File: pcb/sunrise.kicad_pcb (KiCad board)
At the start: 2 copper layers, 6 parts, among them J1 Conn_01x15_Female, J3 Conn_01x04_Female, Q1 TSM2302CX, Q2 TSM2302CX, Q3 TSM2302CX

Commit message: Updated schematic and footprints
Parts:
- added J2: Conn_01x15_Female, Connector_PinSocket_2.54mm:PinSocket_1x15_P2.54mm_Vertical, F.Cu at (116.8, 97.8)
- added R2: R, Resistor_SMD:R_0805_2012Metric, F.Cu at (95.2, 85.1)
- added R3: R, Resistor_SMD:R_0805_2012Metric, F.Cu at (87.6, 85.1)
- added U1: MCP1703A-5002_SOT223, Package_TO_SOT_SMD:SOT-223-3_TabPin2, F.Cu at (119.4, 87.6)
- J1: footprint Connector_PinHeader_1.27mm:PinHeader_1x15_P1.27mm_Vertical -> Connector_PinSocket_2.54mm:PinSocket_1x15_P2.54mm_Vertical
- moved J1 59.2 mm to (116.8, 77.5), turned to -90 degrees
- moved R1 50.6 mm to (102.9, 85.1), turned to 180 degrees
- moved Q1 49.4 mm to (102.9, 90.2)
- moved Q2 48.3 mm to (95.2, 90.2)
- moved Q3 44.5 mm to (87.6, 90.2)
- moved J3 22.9 mm to (80.0, 86.4)
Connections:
- Q2 pad 1: /Green_IO -> Net-(Q2-Pad1)
- Q3 pad 1: /Blue_IO -> Net-(Q3-Pad1)
- R1 pad 1: /Red_IO -> unconnected-(R1-Pad1)
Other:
- board outline added: 52.1 x 27.9 mm

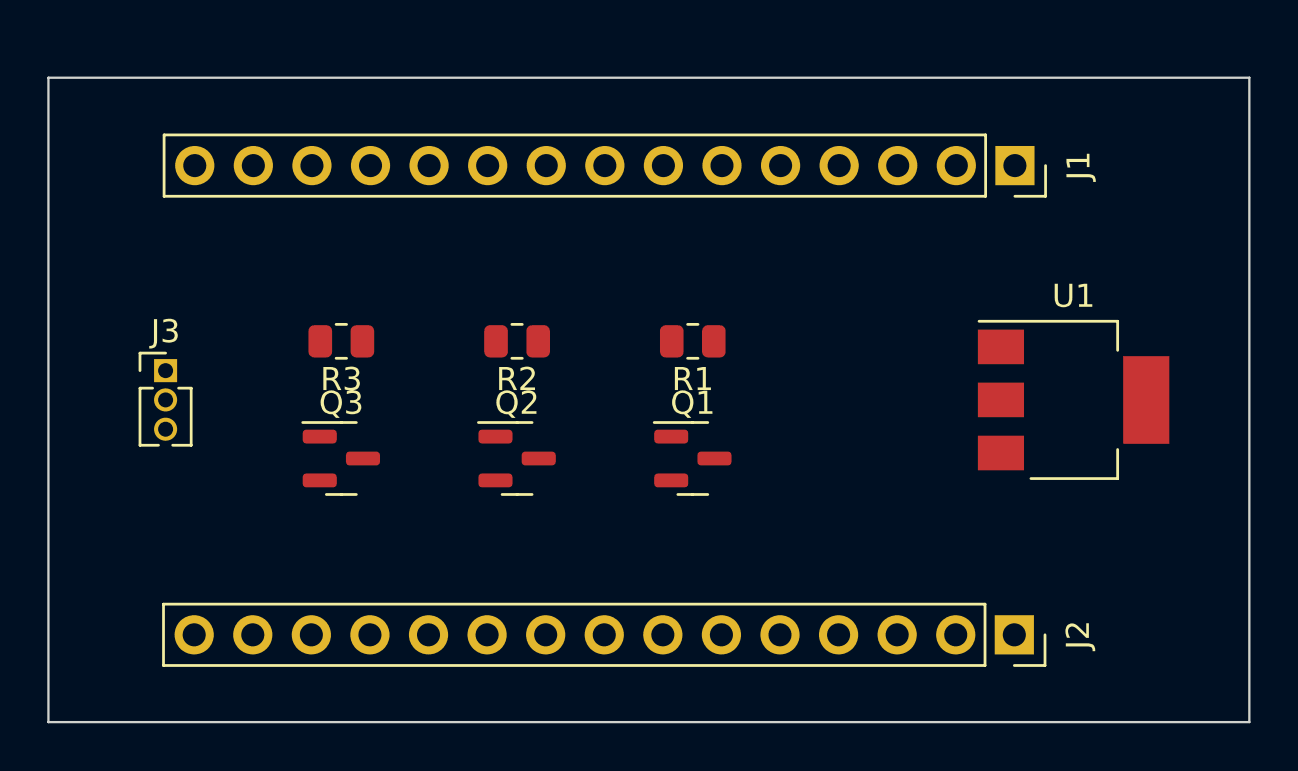
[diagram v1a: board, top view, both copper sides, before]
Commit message: Corrected schematic and finished layout
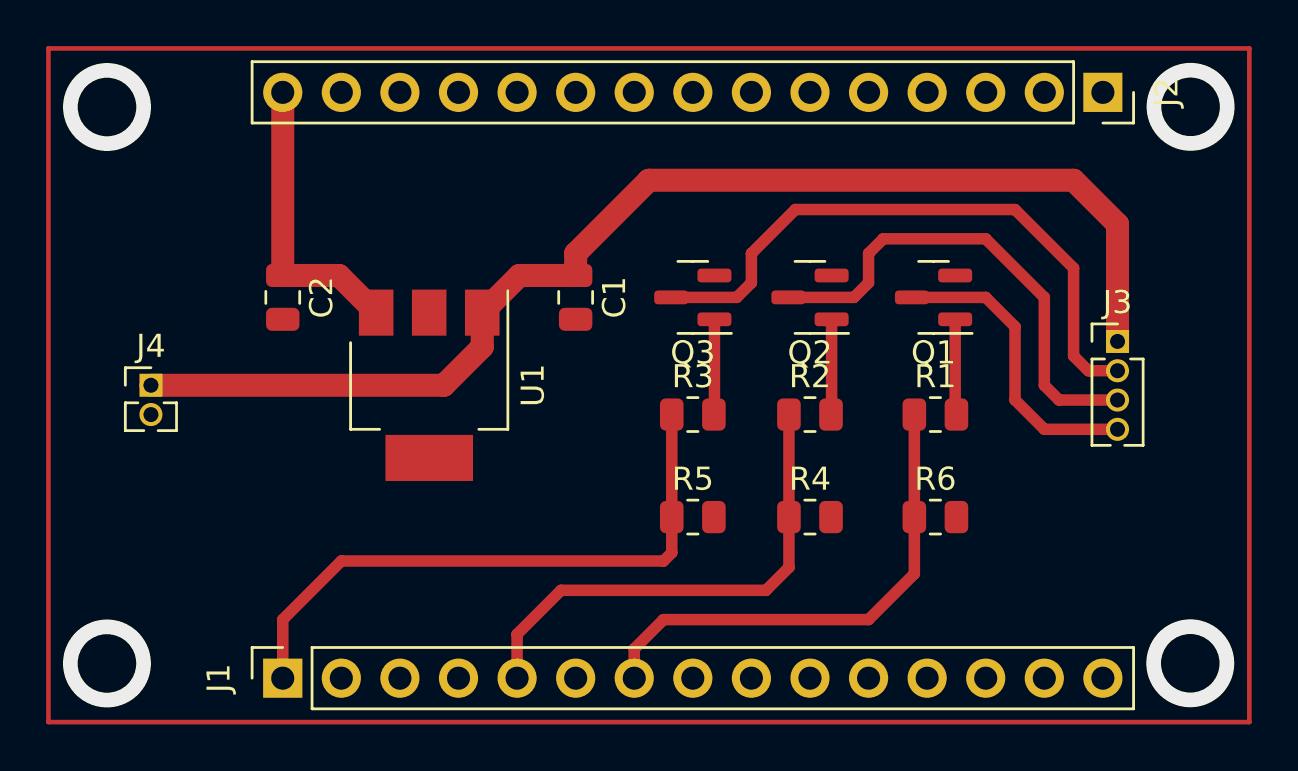
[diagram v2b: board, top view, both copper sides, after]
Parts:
- added C1: 10uF, Capacitor_SMD:C_0805_2012Metric, F.Cu at (97.8, 83.2)
- added C2: 10uF, Capacitor_SMD:C_0805_2012Metric, F.Cu at (85.1, 83.2)
- added J4: Conn_01x02_Female, Connector_PinHeader_1.27mm:PinHeader_1x02_P1.27mm_Vertical, F.Cu at (79.4, 87.0)
- added R4: 5k6, Resistor_SMD:R_0805_2012Metric, F.Cu at (108.0, 92.7)
- added R5: 5k6, Resistor_SMD:R_0805_2012Metric, F.Cu at (102.9, 92.7)
- added R6: 5k6, Resistor_SMD:R_0805_2012Metric, F.Cu at (113.4, 92.7)
- J3: footprint Connector_PinHeader_1.27mm:PinHeader_1x03_P1.27mm_Vertical -> Connector_PinHeader_1.27mm:PinHeader_1x04_P1.27mm_Vertical
- R1, R2, R3: value R -> 560
- moved J3 41.3 mm to (121.3, 85.1)
- moved J1 38.8 mm to (85.1, 99.7), turned to 90 degrees
- moved U1 27.9 mm to (91.4, 87.0), turned to -90 degrees
- moved J2 23.8 mm to (120.7, 74.3)
- moved Q3 16.8 mm to (102.9, 83.2), turned to 180 degrees
- moved R3 15.6 mm to (102.9, 88.3), turned to 0 degrees
- moved Q2 14.5 mm to (108.0, 83.2), turned to 180 degrees
- moved R2 13.1 mm to (108.0, 88.3), turned to 0 degrees
- moved Q1 12.6 mm to (113.3, 83.2), turned to 180 degrees
- moved R1 11.0 mm to (113.4, 88.3), turned to 0 degrees
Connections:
- J1 pad 1: /Red_IO -> /BLUE_IO
- J1 pad 5: unconnected-(J1-Pad5) -> /GREEN_IO
- J1 pad 7: unconnected-(J1-Pad7) -> /RED_IO
- J2 pad 14: unconnected-(J2-Pad14) -> GND
- J2 pad 15: unconnected-(J2-Pad15) -> +5V
- Q1 pad 3: Net-(Q1-Pad3) -> Net-(J3-Pad4)
- R1 pad 1: unconnected-(R1-Pad1) -> /RED_IO
- R2 pad 1: unconnected-(R2-Pad1) -> /GREEN_IO
- R3 pad 1: unconnected-(R3-Pad1) -> /BLUE_IO
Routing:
- net +12V: track 0.00 -> 52.9 mm
- net Net-(J3-Pad2): track 0.00 -> 26.8 mm
- net /BLUE_IO: track 0.00 -> 26.6 mm
- net /RED_IO: track 0.00 -> 21.7 mm
- net /GREEN_IO: track 0.00 -> 21.5 mm
- net Net-(J3-Pad3): track 0.00 -> 21.2 mm
- net Net-(J3-Pad4): track 0.00 -> 13.1 mm
- net +5V: track 0.00 -> 12.7 mm
- net Net-(Q1-Pad1): track 0.00 -> 4.15 mm
- net Net-(Q3-Pad1): track 0.00 -> 4.14 mm
- net Net-(Q2-Pad1): track 0.00 -> 4.14 mm
- net (no net): vias 0 -> 4
- added copper zone on F.Cu, net GND
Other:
- board outline removed

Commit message: Final
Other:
- board outline added: 52.1 x 29.2 mm
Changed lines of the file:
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@@
     (property "Sheetname" "")
     (attr smd)
-    (fp_text reference "R6" (at 0 -1.65) (layer "F.SilkS")
+    (fp_text reference "R6" (at -2.6435 0) (layer "F.SilkS")
       (effects (font (size 1 1) (thickness 0.15)))
     )
@@
     (property "Sheetname" "")
     (attr smd)
-    (fp_text reference "R3" (at 0 -1.65) (layer "F.SilkS")
+    (fp_text reference "R3" (at -3.175 0) (layer "F.SilkS")
       (effects (font (size 1 1) (thickness 0.15)))
     )
@@
     (property "Sheetname" "")
     (attr smd)
-    (fp_text reference "R2" (at 0 -1.65) (layer "F.SilkS")
+    (fp_text reference "R2" (at -2.54 0) (layer "F.SilkS")
       (effects (font (size 1 1) (thickness 0.15)))
     )
@@
     (property "Sheetname" "")
     (attr smd)
-    (fp_text reference "R5" (at 0 -1.65) (layer "F.SilkS")
+    (fp_text reference "R5" (at -3.175 0) (layer "F.SilkS")
       (effects (font (size 1 1) (thickness 0.15)))
     )
@@
     (property "Sheetname" "")
     (attr smd)
-    (fp_text reference "R4" (at 0 -1.65) (layer "F.SilkS")
+    (fp_text reference "R4" (at -2.54 0) (layer "F.SilkS")
       (effects (font (size 1 1) (thickness 0.15)))
     )
@@
     (property "Sheetname" "")
     (attr smd)
-    (fp_text reference "R1" (at 0 -1.65) (layer "F.SilkS")
+    (fp_text reference "R1" (at -2.6435 0) (layer "F.SilkS")
       (effects (font (size 1 1) (thickness 0.15)))
     )
@@
     )
   )
-  (gr_rect (start 74.93 101.6) (end 127 72.39) (layer "F.Cu") (width 0.2) (fill none))
+  (gr_rect (start 74.93 101.6) (end 127 72.39) (layer "Edge.Cuts") (width 0.2) (fill none))
   (via (at 124.452319 74.922319) (size 3.81) (drill 2.54) (layers "F.Cu" "B.Cu") (free) (net 0))
   (via (at 124.438991 99.049495) (size 3.81) (drill 2.54) (layers "F.Cu" "B.Cu") (free) (net 0))

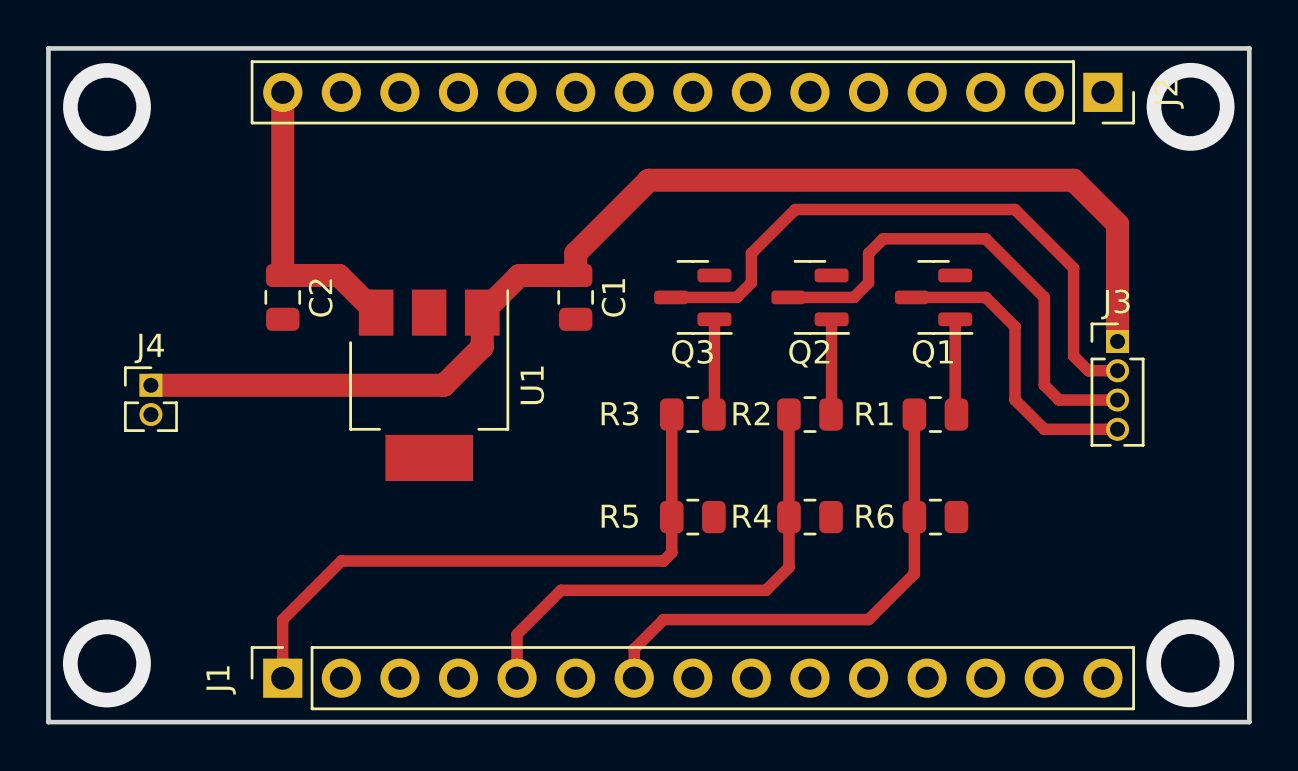
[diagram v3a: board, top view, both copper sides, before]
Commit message: Added IR receiver
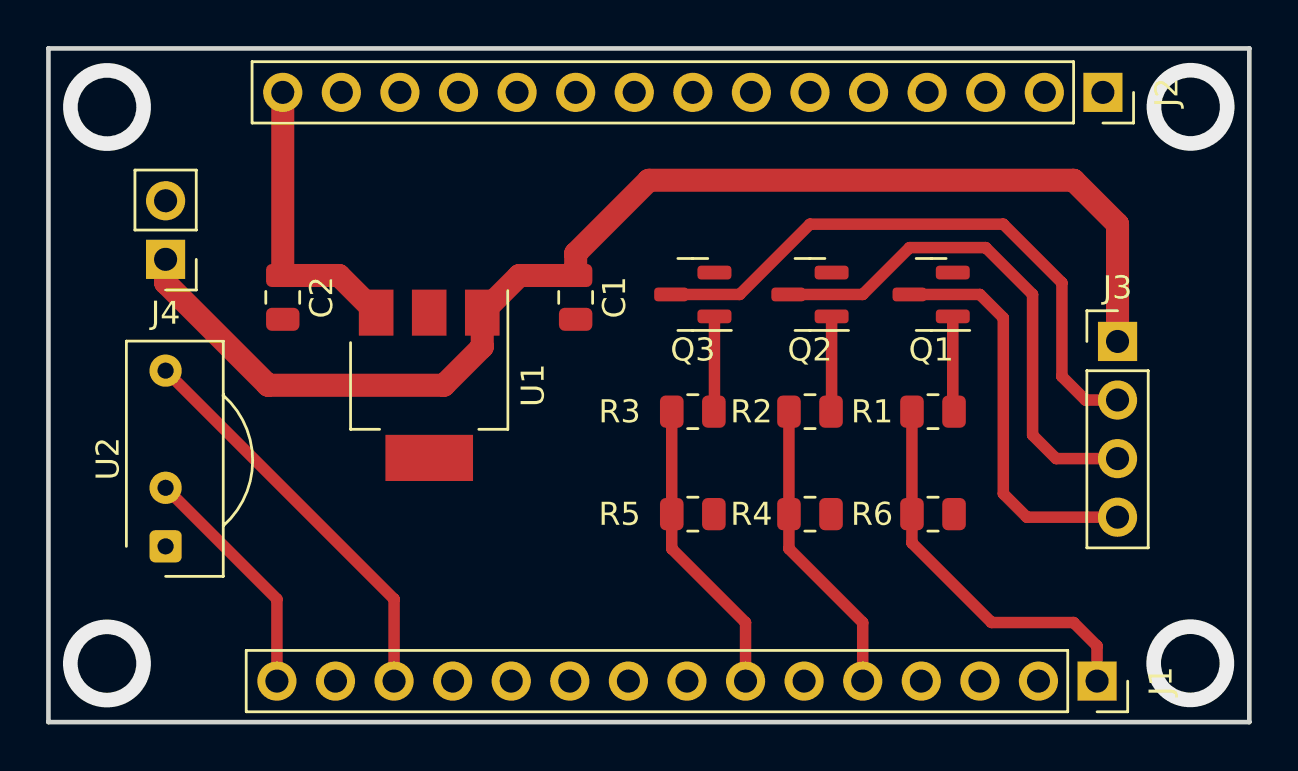
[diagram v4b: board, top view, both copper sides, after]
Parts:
- added U2: TSOP312xx, OptoDevice:Vishay_CAST-3Pin, F.Cu at (80.0, 94.0)
- J3: footprint Connector_PinHeader_1.27mm:PinHeader_1x04_P1.27mm_Vertical -> Connector_PinHeader_2.54mm:PinHeader_1x04_P2.54mm_Vertical
- J4: footprint Connector_PinHeader_1.27mm:PinHeader_1x02_P1.27mm_Vertical -> Connector_PinHeader_2.54mm:PinHeader_1x02_P2.54mm_Vertical
- moved J1 35.3 mm to (120.4, 99.8), turned to -90 degrees
- moved J4 5.50 mm to (80.0, 81.5), turned to 180 degrees
- moved Q1 0.16 mm to (113.2, 83.1)
- moved R1 0.16 mm to (113.3, 88.1)
- moved R6 0.16 mm to (113.3, 92.6)
- moved Q2 0.13 mm to (108.0, 83.1)
- moved Q3 0.13 mm to (102.9, 83.1)
- moved R2 0.13 mm to (108.0, 88.1)
- moved R3 0.13 mm to (102.9, 88.1)
- moved R4 0.13 mm to (108.0, 92.6)
- moved R5 0.13 mm to (102.9, 92.6)
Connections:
- J1 pad 1: /BLUE_IO -> /RED_IO
- J1 pad 13: unconnected-(J1-Pad13) -> /IR_D
- J1 pad 14: unconnected-(J1-Pad14) -> GND
- J1 pad 15: unconnected-(J1-Pad15) -> /+3.3V
- J1 pad 7: /RED_IO -> /BLUE_IO
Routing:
- net /IR_D: track 0.00 -> 17.6 mm
- net /BLUE_IO: track 26.6 -> 13.0 mm
- net /+3.3V: track 0.00 -> 10.4 mm
- net /GREEN_IO: track 21.5 -> 13.0 mm
- net /RED_IO: track 21.7 -> 17.1 mm
- net Net-(J3-Pad4): track 13.1 -> 17.5 mm
- net +12V: track 52.9 -> 55.1 mm
- net Net-(J3-Pad3): track 21.2 -> 22.5 mm
- net Net-(J3-Pad2): track 26.8 -> 26.2 mm
- removed copper zone on F.Cu, net GND

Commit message: Updated pcb
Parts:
- moved U2 1.02 mm to (80.0, 95.0)
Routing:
- added copper zone on F.Cu, net GND
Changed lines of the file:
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@@
   )
   (footprint "OptoDevice:Vishay_CAST-3Pin" (layer "F.Cu")
-    (at 80.01 93.98 90)
+    (at 80.01 94.996 90)
     (descr "IR Receiver Vishay TSOP-xxxx, CAST package, see https://www.vishay.com/docs/82493/tsop311.pdf")
     (tags "IRReceiverVishayTSOP-xxxx CAST")
@@
   (segment (start 92.075 86.995) (end 93.74 85.33) (width 1) (layer "F.Cu") (net 7))
   (segment (start 119.38 78.105) (end 121.285 80.01) (width 1) (layer "F.Cu") (net 7))
-  (segment (start 80.01 86.36) (end 89.916 96.266) (width 0.5) (layer "F.Cu") (net 18))
-  (segment (start 89.916 96.266) (end 89.916 99.822) (width 0.5) (layer "F.Cu") (net 18))
-  (segment (start 80.01 91.44) (end 84.836 96.266) (width 0.5) (layer "F.Cu") (net 19))
-  (segment (start 84.836 96.266) (end 84.836 99.822) (width 0.5) (layer "F.Cu") (net 19))
+  (segment (start 89.916 96.012) (end 89.916 99.822) (width 0.5) (layer "F.Cu") (net 18))
+  (segment (start 80.01 87.376) (end 81.28 87.376) (width 0.5) (layer "F.Cu") (net 18))
+  (segment (start 81.28 87.376) (end 89.916 96.012) (width 0.5) (layer "F.Cu") (net 18))
+  (segment (start 80.01 92.456) (end 82.296 92.456) (width 0.5) (layer "F.Cu") (net 19))
+  (segment (start 82.296 92.456) (end 84.836 94.996) (width 0.5) (layer "F.Cu") (net 19))
+  (segment (start 84.836 94.996) (end 84.836 99.822) (width 0.5) (layer "F.Cu") (net 19))
   (segment (start 103.8075 88.113) (end 103.7825 88.138) (width 0.5) (layer "F.Cu") (net 20))
   (segment (start 103.8075 84.008) (end 103.8075 88.113) (width 0.5) (layer "F.Cu") (net 20))
@@
   (segment (start 85.09 82.235) (end 85.09 74.295) (width 1) (layer "F.Cu") (net 24))
   (segment (start 87.53 82.235) (end 89.14 83.845) (width 1) (layer "F.Cu") (net 24))
+  (zone (net 1) (net_name "GND") (layer "F.Cu") (hatch edge 0.508)
+    (connect_pads (clearance 0.12))
+    (min_thickness 0.254) (filled_areas_thickness no)
+    (fill yes (thermal_gap 0.508) (thermal_bridge_width 0.508))
+    (polygon
+      (pts
+        (xy 127 101.6)
+        (xy 74.93 101.6)
+        (xy 74.93 72.39)
+        (xy 127 72.39)
+      )
+    )
+  )
 )

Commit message: Final layout
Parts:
- added R7: 10k, Resistor_SMD:R_0805_2012Metric, F.Cu at (89.9, 96.8)
- added R8: 10k, Resistor_SMD:R_0805_2012Metric, F.Cu at (120.4, 95.4)
- added SW1: SW_SPDT, MattisLib:SS 13PLP, F.Cu at (123.2, 86.9)
- moved J3 3.77 mm to (118.1, 83.1)
- moved R1 1.63 mm to (111.7, 88.1)
- moved R6 1.63 mm to (111.7, 92.6)
- moved Q1 1.63 mm to (111.6, 83.1)
- moved Q2 1.63 mm to (106.3, 83.1)
- moved Q3 1.63 mm to (101.2, 83.1)
- moved R2 1.63 mm to (106.3, 88.1)
- moved R3 1.63 mm to (101.2, 88.1)
- moved R4 1.63 mm to (106.3, 92.6)
- moved R5 1.63 mm to (101.2, 92.6)
- moved C1 0.76 mm to (97.0, 83.2)
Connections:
- J1 pad 1: /RED_IO -> /ALARM_EN
- J1 pad 2: unconnected-(J1-Pad2) -> /RED_IO
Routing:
- net Net-(R7-Pad2): track 0.00 -> 51.2 mm
- net /ALARM_EN: track 0.00 -> 15.4 mm
- net +12V: track 55.1 -> 48.8 mm
- net Net-(R8-Pad2): track 0.00 -> 5.30 mm
- net /+3.3V: track 10.7 -> 15.6 mm
- net Net-(J3-Pad4): track 17.5 -> 13.8 mm
- net Net-(J3-Pad3): track 22.5 -> 19.5 mm
- net Net-(J3-Pad2): track 26.2 -> 23.3 mm
- net /BLUE_IO: track 13.0 -> 14.7 mm
- net /GREEN_IO: track 13.0 -> 14.6 mm
- net /IR_D: track 17.3 -> 18.3 mm
- net /RED_IO: track 17.1 -> 16.5 mm
